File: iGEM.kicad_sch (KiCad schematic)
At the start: 55 parts, among them IC1 TMCS1107A1BQDRQ1, IC2 MCP4642-502E_UN, IC3 SN74LVC2G08IDCTRQ1, J1 COIL, J2 Conn_01x03, J3 Conn_01x02, J4 Conn_01x03, J5 Conn_01x03, J6 Conn_02x03_Odd_Even, M1 Fan, Q1 TIP122, Q2 IPD042P03L3GATMA1, Q3 IRL1404ZSTRLPBF, Q4 D44VH, Q5 IPD042P03L3GATMA1, Q6 TIP122, Q7 D44VH, Q8 IRL1404ZSTRLPBF, U1 ADC101C021CIMK, U2 ATtiny412-SS, U3 SN74LVC1G04DBVR, U4 FAN3268TMX, U5 FAN3268TMX

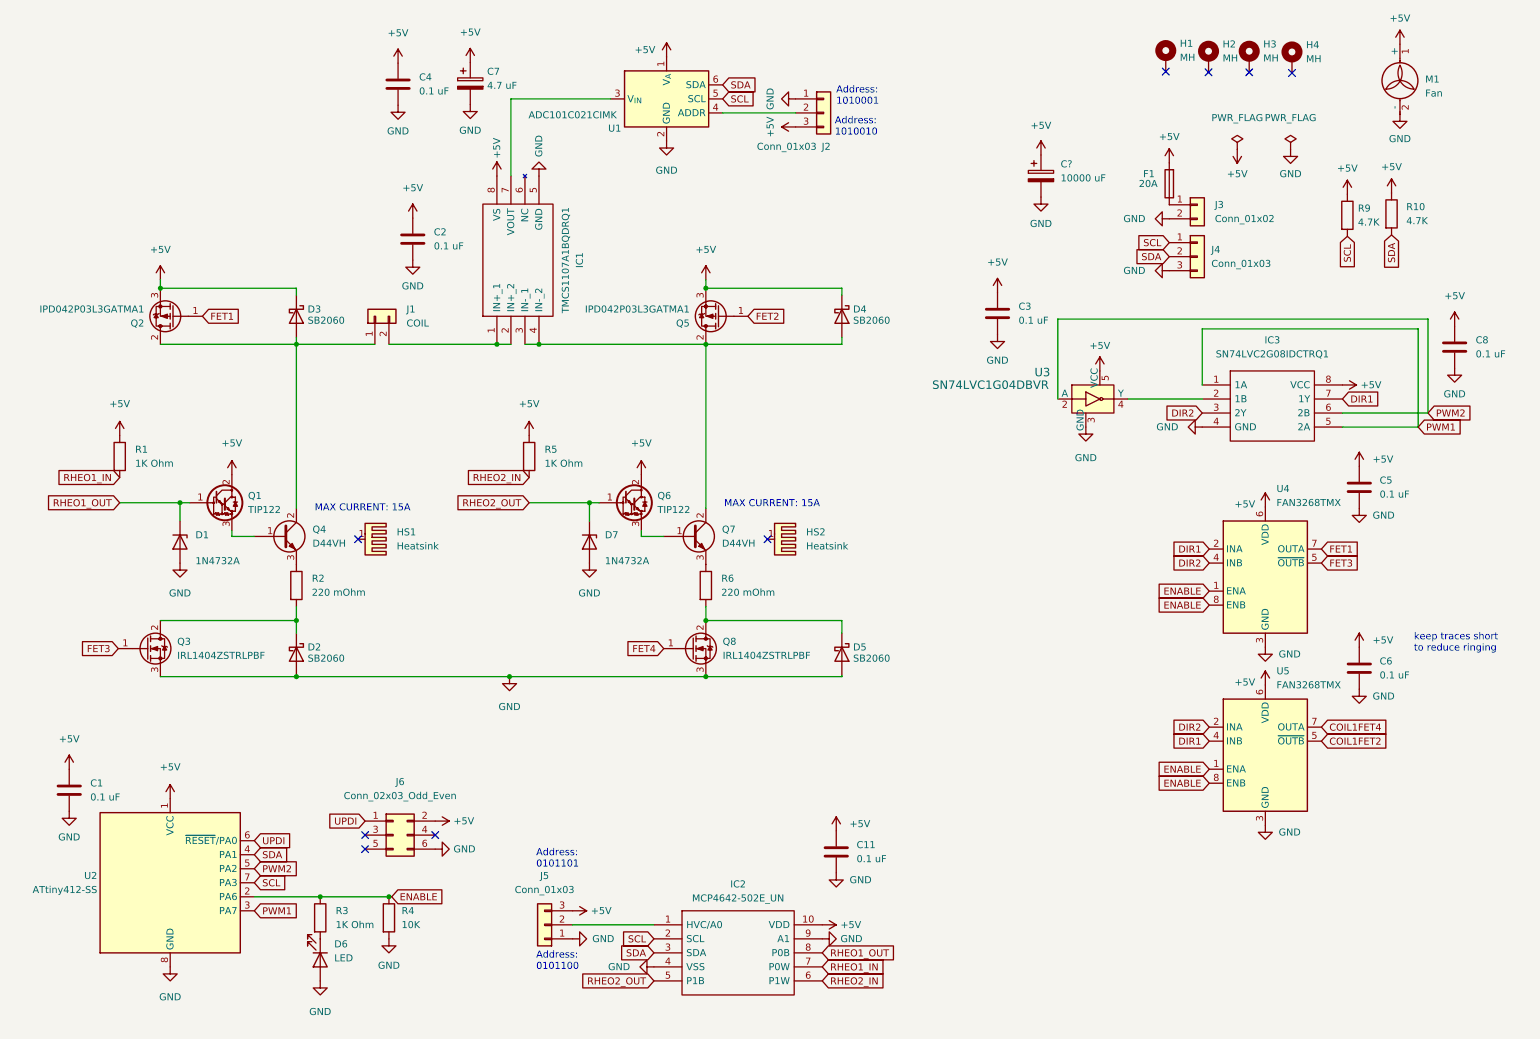
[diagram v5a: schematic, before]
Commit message: Changes to improve thermals and layout
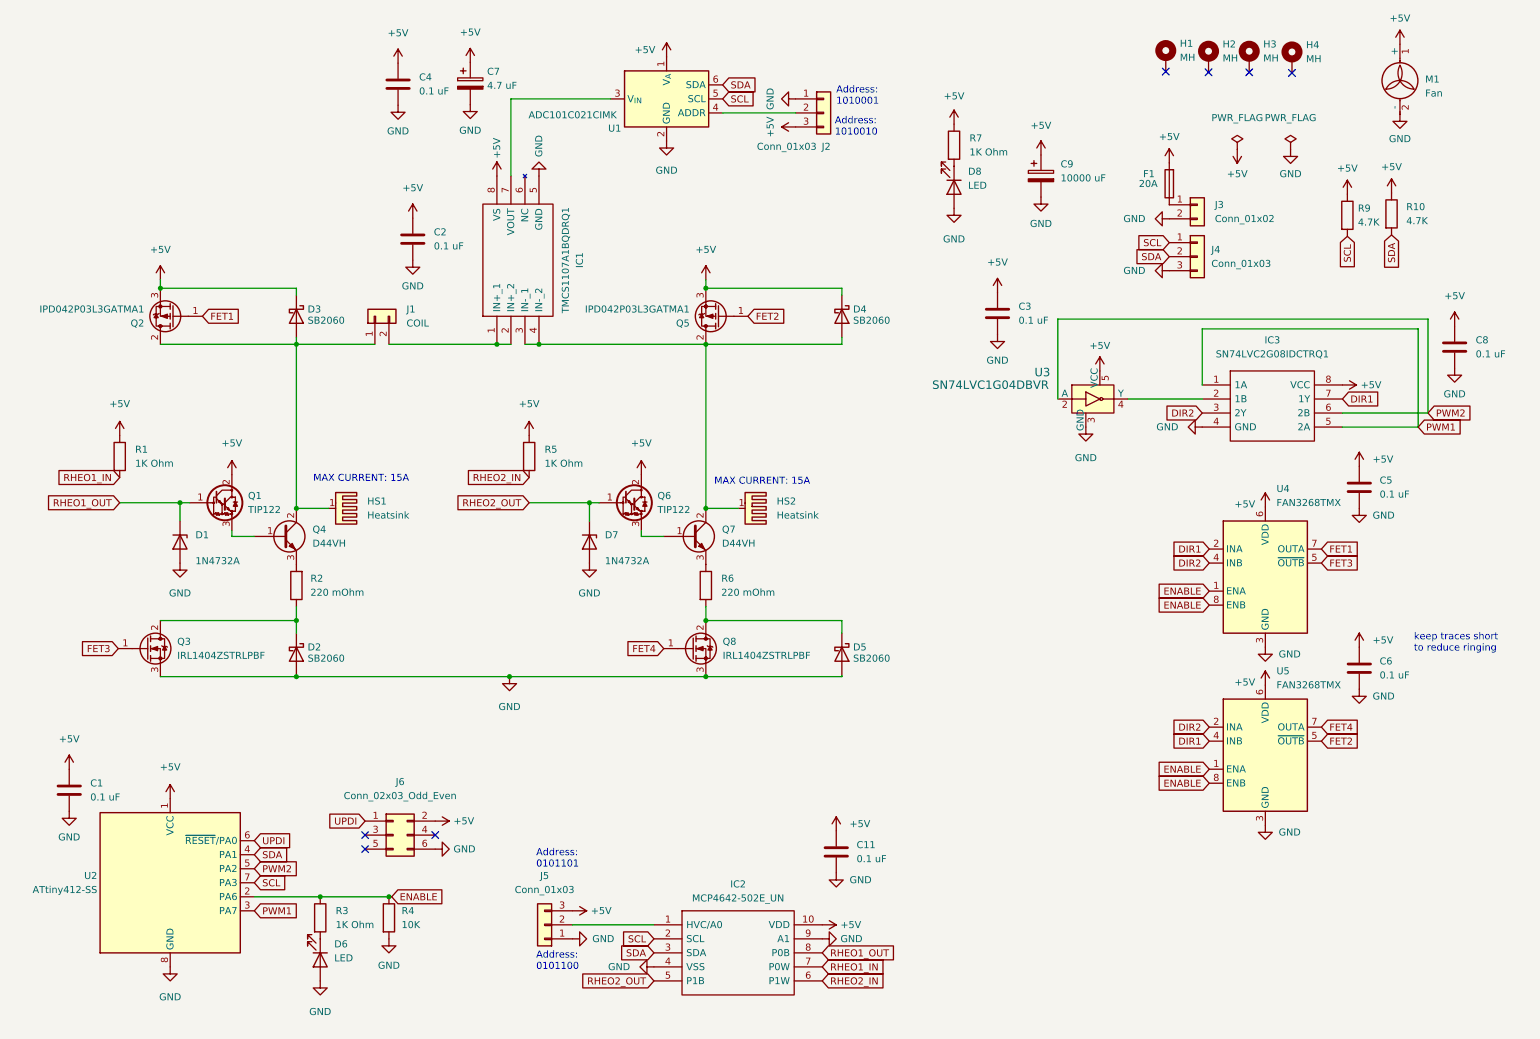
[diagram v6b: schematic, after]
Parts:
- added D8: LED, LED_SMD:LED_0805_2012Metric_Pad1.15x1.40mm_HandSolder, symbol Device:LED
- added R7: 1K Ohm, Resistor_SMD:R_0805_2012Metric_Pad1.20x1.40mm_HandSolder, symbol Device:R
- gave numbers to parts that had none: 1
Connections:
- net COIL1FET2 is gone; now on net FET2: U5.5 (~{OUTB})
- net COIL1FET4 is gone; now on net FET4: U5.7 (OUTA)
- net +5V: now also R7.1
- net GND: now also D8.2 (A)
- net at D4.2 (A), IC1.3 (IN-_1), IC1.4 (IN-_2)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: now also HS2.1
- net at D3.2 (A), J1.1 (Pin_1), Q2.2 (D)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: now also HS1.1
- net at Q4.3 (E): now also R2.2; no longer R2.1
- net at D2.1 (K), Q3.2 (D): now also R2.1; no longer R2.2
- new net: D8.1 (K), R7.2
- no-connect marks 9 -> 7
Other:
- moved on the sheet: HS1, HS2, R2

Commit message: update layout and heatsink
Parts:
- HS1, HS2: footprint Heatsink:Heatsink_AAVID_576802B03900G -> Heatsink:Heatsink_Fischer_SK104-STC-STIC_35x13mm_2xDrill2.5mm; DigiKey 6021BG-ND -> HS403-ND
- Q1, Q6: footprint Package_TO_SOT_THT:TO-220-3_Vertical -> Package_TO_SOT_THT:TO-220-3_Horizontal_TabDown
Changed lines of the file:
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@@
       (effects (font (size 1.27 1.27)) (justify left))
     )
-    (property "Footprint" "Package_TO_SOT_THT:TO-220-3_Vertical" (id 2) (at 54.356 104.521 0)
+    (property "Footprint" "Package_TO_SOT_THT:TO-220-3_Horizontal_TabDown" (id 2) (at 54.356 104.521 0)
       (effects (font (size 1.27 1.27) italic) (justify left) hide)
     )
@@
       (effects (font (size 1.27 1.27)) (justify left))
     )
-    (property "Footprint" "Heatsink:Heatsink_AAVID_576802B03900G" (id 2) (at 70.612 103.9368 0)
+    (property "Footprint" "Heatsink:Heatsink_Fischer_SK104-STC-STIC_35x13mm_2xDrill2.5mm" (id 2) (at 70.612 103.9368 0)
       (effects (font (size 1.27 1.27)) hide)
     )
@@
       (effects (font (size 1.27 1.27)) hide)
     )
-    (property "DigiKey" "6021BG-ND" (id 4) (at 71.882 103.632 90)
+    (property "DigiKey" "HS403-ND" (id 4) (at 71.882 103.632 90)
       (effects (font (size 1.27 1.27)) hide)
     )
@@
       (effects (font (size 1.27 1.27)) (justify left))
     )
-    (property "Footprint" "Package_TO_SOT_THT:TO-220-3_Vertical" (id 2) (at 128.524 104.521 0)
+    (property "Footprint" "Package_TO_SOT_THT:TO-220-3_Horizontal_TabDown" (id 2) (at 128.524 104.521 0)
       (effects (font (size 1.27 1.27) italic) (justify left) hide)
     )
@@
       (effects (font (size 1.27 1.27)) (justify left))
     )
-    (property "Footprint" "Heatsink:Heatsink_AAVID_576802B03900G" (id 2) (at 144.78 103.9368 0)
+    (property "Footprint" "Heatsink:Heatsink_Fischer_SK104-STC-STIC_35x13mm_2xDrill2.5mm" (id 2) (at 144.78 103.9368 0)
       (effects (font (size 1.27 1.27)) hide)
     )
@@
       (effects (font (size 1.27 1.27)) hide)
     )
-    (property "DigiKey" "6021BG-ND" (id 4) (at 146.05 103.632 90)
+    (property "DigiKey" "HS403-ND" (id 4) (at 146.05 103.632 90)
       (effects (font (size 1.27 1.27)) hide)
     )
@@
     )
     (path "/51879485-f54c-4d64-8de1-5fd9b52a4051"
-      (reference "HS1") (unit 1) (value "Heatsink") (footprint "Heatsink:Heatsink_AAVID_576802B03900G")
+      (reference "HS1") (unit 1) (value "Heatsink") (footprint "Heatsink:Heatsink_Fischer_SK104-STC-STIC_35x13mm_2xDrill2.5mm")
     )
     (path "/fd1f3134-e94c-4ccc-9125-06d251fe0321"
-      (reference "HS2") (unit 1) (value "Heatsink") (footprint "Heatsink:Heatsink_AAVID_576802B03900G")
+      (reference "HS2") (unit 1) (value "Heatsink") (footprint "Heatsink:Heatsink_Fischer_SK104-STC-STIC_35x13mm_2xDrill2.5mm")
     )
     (path "/e46d9648-bbc2-4e10-a2da-8923352095b0"
@@
     )
     (path "/4b59aaf5-2612-4b64-b615-ddf78dad43ca"
-      (reference "Q1") (unit 1) (value "TIP122") (footprint "Package_TO_SOT_THT:TO-220-3_Vertical")
+      (reference "Q1") (unit 1) (value "TIP122") (footprint "Package_TO_SOT_THT:TO-220-3_Horizontal_TabDown")
     )
     (path "/f8bb0d9a-e5ac-4c1f-87fb-a3fb9a596c98"
@@
     )
     (path "/94b8931b-1a18-46c9-a522-d5b95f3e23d9"
-      (reference "Q6") (unit 1) (value "TIP122") (footprint "Package_TO_SOT_THT:TO-220-3_Vertical")
+      (reference "Q6") (unit 1) (value "TIP122") (footprint "Package_TO_SOT_THT:TO-220-3_Horizontal_TabDown")
     )
     (path "/ba4cc950-79f1-4cdf-8f3e-2b38f0e15fde"

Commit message: Adding BOM 'iGEM.csv'
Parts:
- IC2: DigiKey (none) -> MCP4642-502E/UN-ND
- IC3: DigiKey (none) -> 296-36980-1-ND
- J2, J5, J6: now left out of the parts list
- Q2, Q5: DigiKey (none) -> IPD042P03L3GATMA1CT-ND
- U2: DigiKey (none) -> ATTINY412-SSN-ND
- U3: DigiKey (none) -> 296-11599-1-ND
- U4, U5: DigiKey (none) -> FAN3268TMXCT-ND
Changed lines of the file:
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@@
   )
   (symbol (lib_id "Connector_Generic:Conn_02x03_Odd_Even") (at 81.026 162.814 0) (unit 1)
-    (in_bom yes) (on_board yes) (fields_autoplaced)
+    (in_bom no) (on_board yes) (fields_autoplaced)
     (property "Reference" "J6" (id 0) (at 82.296 153.162 0))
     (property "Value" "Conn_02x03_Odd_Even" (id 1) (at 82.296 155.702 0))
@@
   )
   (symbol (lib_id "Connector_Generic:Conn_01x03") (at 159.004 32.004 0) (unit 1)
-    (in_bom yes) (on_board yes)
+    (in_bom no) (on_board yes)
     (property "Reference" "J2" (id 0) (at 160.2741 38.1 0)
       (effects (font (size 1.27 1.27)) (justify right))
@@
     (property "Status" "Active" (id 12) (at 214.122 53.34 0)
       (effects (font (size 1.524 1.524)) (justify left) hide)
+    )
+    (property "DigiKey" "296-11599-1-ND" (id 13) (at 209.042 83.82 0)
+      (effects (font (size 1.27 1.27)) hide)
     )
     (pin "1")
@@
     )
     (property "Datasheet" "https://www.onsemi.com/pdf/datasheet/fan3268-d.pdf" (id 3) (at 239.014 145.796 0)
+      (effects (font (size 1.27 1.27)) hide)
+    )
+    (property "DigiKey" "FAN3268TMXCT-ND" (id 4) (at 239.014 148.336 0)
       (effects (font (size 1.27 1.27)) hide)
     )
@@
       (effects (font (size 1.27 1.27)) hide)
     )
+    (property "DigiKey" "FAN3268TMXCT-ND" (id 4) (at 239.014 116.078 0)
+      (effects (font (size 1.27 1.27)) hide)
+    )
     (pin "1")
     (pin "2")
@@
       (effects (font (size 1.27 1.27)) hide)
     )
+    (property "DigiKey" "IPD042P03L3GATMA1CT-ND" (id 4) (at 140.208 68.834 0)
+      (effects (font (size 1.27 1.27)) hide)
+    )
     (pin "1")
     (pin "2")
@@
   )
   (symbol (lib_id "Connector_Generic:Conn_01x03") (at 108.458 179.07 180) (unit 1)
-    (in_bom yes) (on_board yes) (fields_autoplaced)
+    (in_bom no) (on_board yes) (fields_autoplaced)
     (property "Reference" "J5" (id 0) (at 108.458 170.18 0))
     (property "Value" "Conn_01x03" (id 1) (at 108.458 172.72 0))
@@
     (property "Arrow Price/Stock" "https://www.arrow.com/en/products/sn74lvc2g08idctrq1/texas-instruments?region=nac" (id 11) (at 249.174 101.6 0)
       (effects (font (size 1.27 1.27)) (justify left) hide)
+    )
+    (property "DigiKey" "296-36980-1-ND" (id 12) (at 227.584 81.28 0)
+      (effects (font (size 1.27 1.27)) hide)
     )
     (pin "1")
@@
       (effects (font (size 1.27 1.27)) hide)
     )
+    (property "DigiKey" "ATTINY412-SSN-ND" (id 4) (at 40.64 171.45 0)
+      (effects (font (size 1.27 1.27)) hide)
+    )
     (pin "1")
     (pin "2")
@@
     (property "Arrow Price/Stock" "" (id 11) (at 154.94 199.39 0)
       (effects (font (size 1.27 1.27)) (justify left) hide)
+    )
+    (property "DigiKey" "MCP4642-502E/UN-ND" (id 12) (at 128.27 179.07 0)
+      (effects (font (size 1.27 1.27)) hide)
     )
     (pin "1")
@@
       (effects (font (size 1.27 1.27)) hide)
     )
+    (property "DigiKey" "IPD042P03L3GATMA1CT-ND" (id 4) (at 41.402 68.834 0)
+      (effects (font (size 1.27 1.27)) hide)
+    )
